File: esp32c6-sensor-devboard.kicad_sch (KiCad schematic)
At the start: 0 parts

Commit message: schem: add esp32-c6 symbol
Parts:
- added C10, C11, C16, C17, C18: 0u1, Capacitor_SMD:C_0402_1005Metric, symbol Device:C
- added C13: 10n, Capacitor_SMD:C_0402_1005Metric, symbol Device:C
- added C14, C15, C9: 1u, Capacitor_SMD:C_0402_1005Metric, symbol Device:C
- added C8: 10u, Capacitor_SMD:C_0402_1005Metric, symbol Device:C
- added L2: 2n7, Inductor_SMD:L_0402_1005Metric, symbol Device:L
- added U1: ESP32-C6, Package_DFN_QFN:QFN-40-1EP_5x5mm_P0.4mm_EP3.6x3.6mm, symbol PCM_Espressif:ESP32-C6
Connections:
- new net: C11.1, L2.2, U1.2 (VDDA3P3), U1.3 (VDDA3P3)
- new net +3V3: C10.1, C13.1, C14.1, C17.1, C18.1, C8.1, C9.1, L2.1, U1.28 (VDDPST2), U1.37 (VDDA1), U1.40 (VDDA2), U1.5 (VDDPST1)
- new net GND: C10.2, C11.2, C13.2, C14.2, C15.2, C16.2, C17.2, C18.2, C8.2, C9.2, U1.41 (GND)
- new net VDD_SPI: C15.1, C16.1, U1.23 (VDD_SPI/GPIO27)

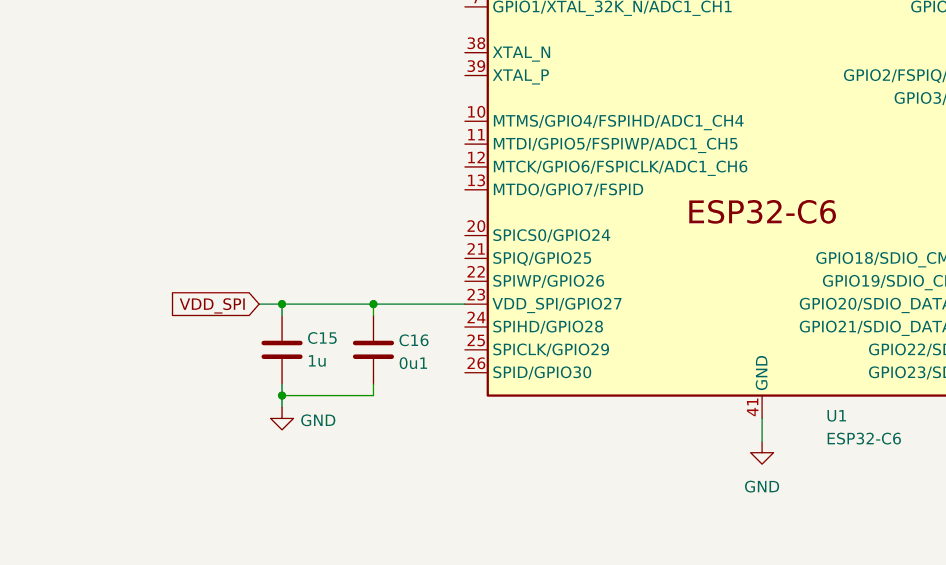
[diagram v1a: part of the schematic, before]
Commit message: schem: add W25Q128JVS 16MB flash
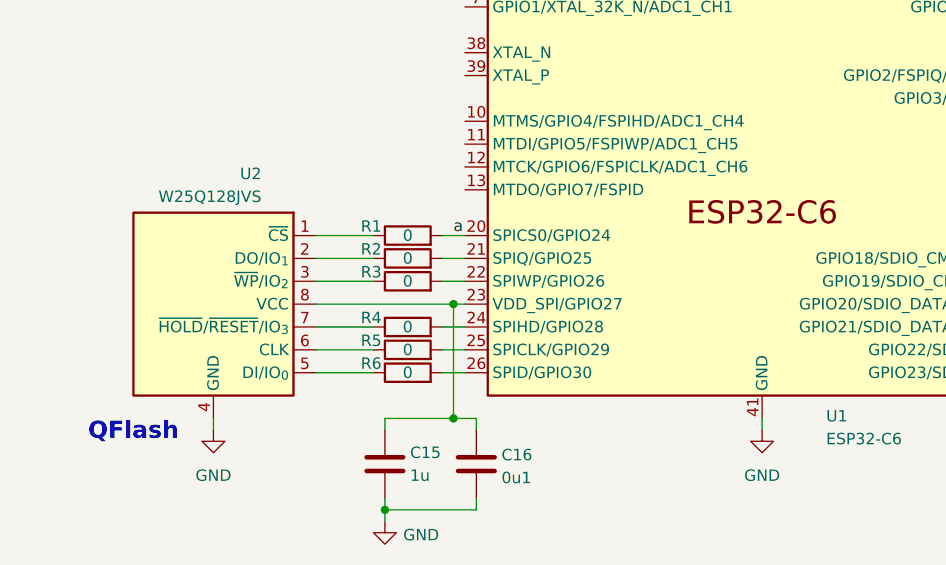
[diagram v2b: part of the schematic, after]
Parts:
- added R1, R2, R3, R4, R5, R6: 0, symbol Device:R
- added U2: W25Q128JVS, Package_SO:SOIC-8_5.3x5.3mm_P1.27mm, symbol Memory_Flash:W25Q128JVS
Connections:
- net GND: now also U2.4 (GND)
- net a: now reaches U1.20 (SPICS0/GPIO24)
- net a: now also R1.2
- net at U1.21 (SPIQ/GPIO25): now also R2.2
- net at U1.22 (SPIWP/GPIO26): now also R3.2
- net at U1.24 (SPIHD/GPIO28): now also R4.2
- net at U1.25 (SPICLK/GPIO29): now also R5.2
- net at U1.26 (SPID/GPIO30): now also R6.2
- net VDD_SPI: no longer names the net of C15.1, C16.1, U1.23 (VDD_SPI/GPIO27)
- net VDD_SPI: now also U2.8 (VCC)
- new net: R2.1, U2.2 (DO/IO_{1})
- new net: R5.1, U2.6 (CLK)
- new net: R1.1, U2.1 (~{CS})
- new net: R3.1, U2.3 (~{WP}/IO_{2})
- new net: R6.1, U2.5 (DI/IO_{0})
- new net: R4.1, U2.7 (~{HOLD}/~{RESET}/IO_{3})
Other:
- note added: "QFlash"
- moved on the sheet: C15, C16

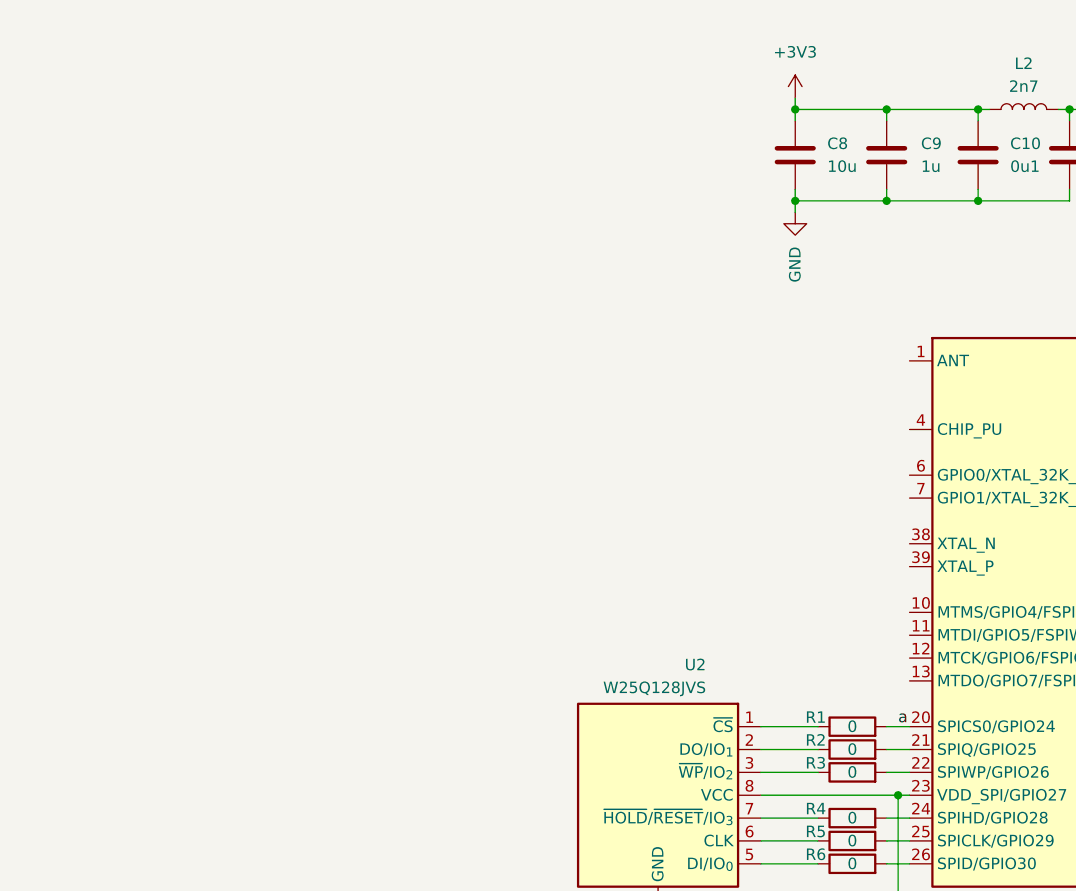
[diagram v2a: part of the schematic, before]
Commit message: schem: add low and high speed crystals
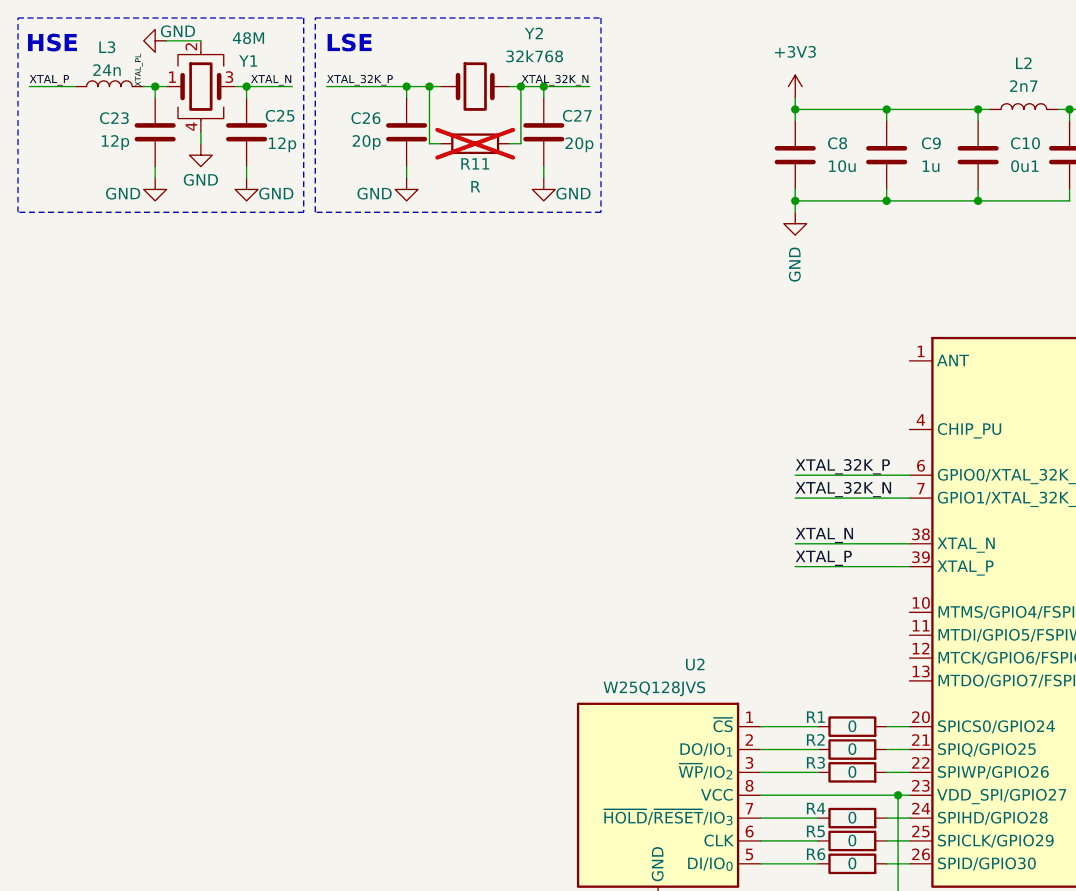
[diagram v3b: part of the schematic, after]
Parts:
- added C23, C25: 12p, Capacitor_SMD:C_0402_1005Metric, symbol Device:C
- added C26, C27: 20p, Capacitor_SMD:C_0402_1005Metric, symbol Device:C
- added L3: 24n, Inductor_SMD:L_0402_1005Metric, symbol Device:L
- added R11: R, Resistor_SMD:R_0603_1608Metric, symbol Device:R
- added Y1: 48M, Crystal:Crystal_SMD_2016-4Pin_2.0x1.6mm, symbol Device:Crystal_GND24
- added Y2: 32k768, Crystal:Crystal_SMD_3215-2Pin_3.2x1.5mm, symbol Device:Crystal
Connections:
- net GND: now also C23.1, C25.2, C26.1, C27.2, Y1.2, Y1.4
- net XTAL_N: now reaches U1.38 (XTAL_N)
- net XTAL_N: now also C25.1, Y1.3
- net XTAL_P: now reaches U1.39 (XTAL_P)
- net XTAL_P: now also L3.1
- net XTAL_32K_P: now reaches U1.6 (GPIO0/XTAL_32K_P/ADC1_CH0)
- net XTAL_32K_P: now also C26.2, R11.1, Y2.1
- net XTAL_32K_N: now reaches U1.7 (GPIO1/XTAL_32K_N/ADC1_CH1)
- net XTAL_32K_N: now also C27.1, R11.2, Y2.2
- net a: no longer names the net of R1.2, U1.20 (SPICS0/GPIO24)
- new net XTAL_PL: C23.2, L3.2, Y1.1
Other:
- note added: "HSE"
- note added: "LSE"

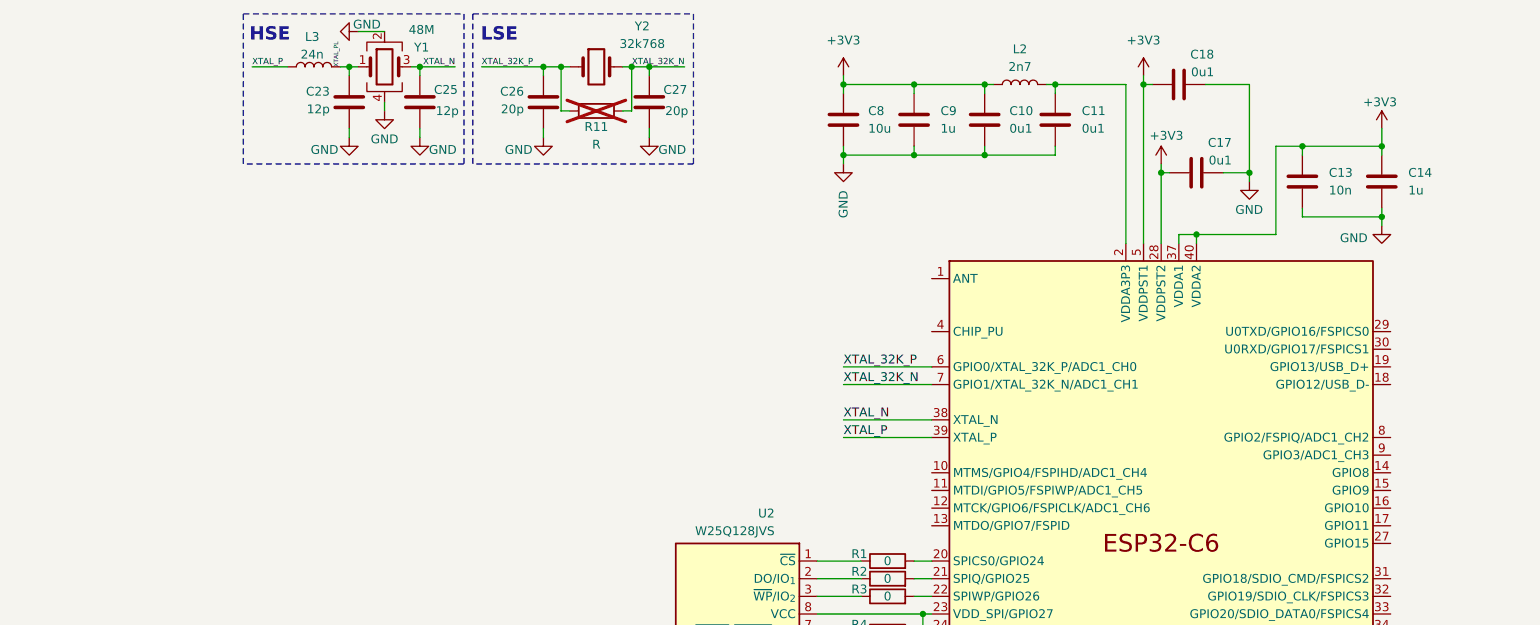
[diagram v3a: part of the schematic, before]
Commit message: schem: add strapping pins and btns
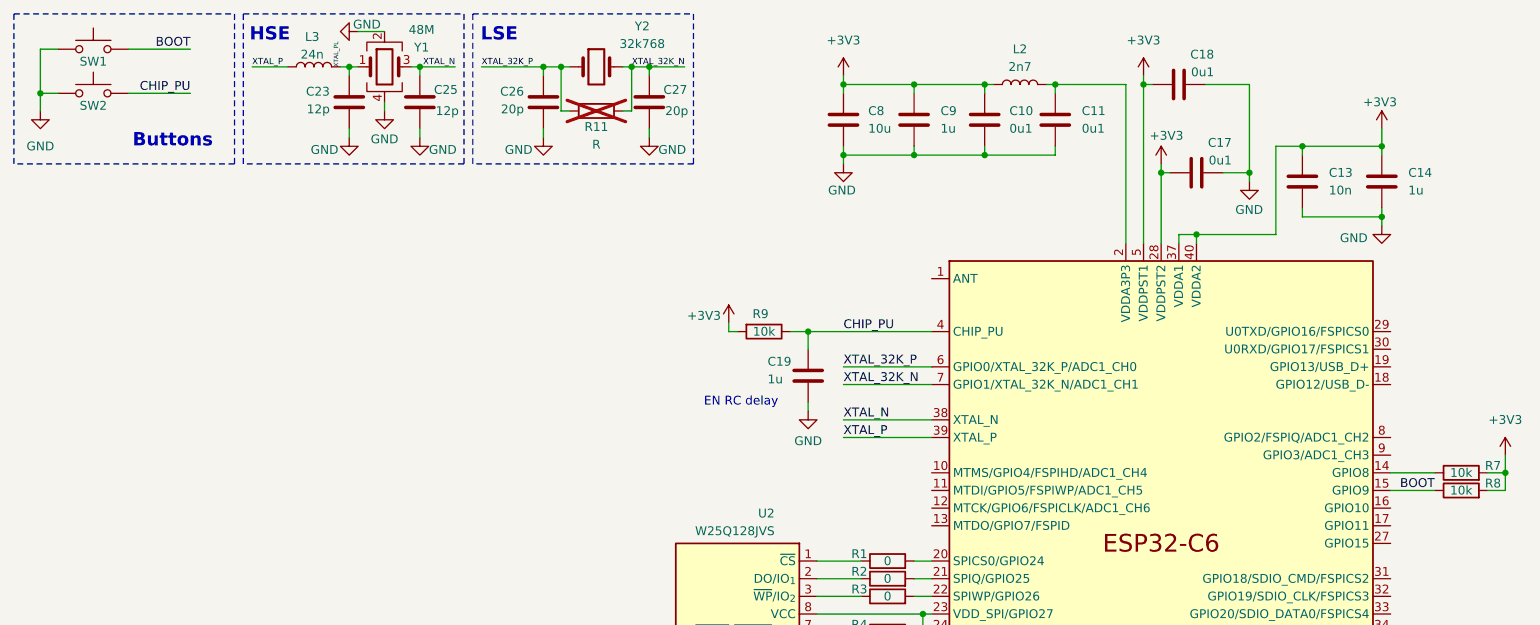
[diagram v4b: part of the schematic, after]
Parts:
- added C19: 1u, Capacitor_SMD:C_0402_1005Metric, symbol Device:C
- added R7, R8, R9: 10k, Resistor_SMD:R_0603_1608Metric, symbol Device:R
- added SW1, SW2: SW_Push, Button_Switch_THT:SW_SPST_Omron_B3F-40xx, symbol Switch:SW_Push
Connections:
- net +3V3: now also R7.2, R8.2, R9.2
- net GND: now also C19.2, SW1.1, SW2.1
- net at U1.14 (GPIO8): now also R7.1
- net BOOT: now reaches U1.15 (GPIO9)
- net BOOT: now also R8.1, SW1.2
- net CHIP_PU: now reaches U1.4 (CHIP_PU)
- net CHIP_PU: now also C19.1, R9.1, SW2.2
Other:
- note added: "Buttons"
- note added: "EN RC delay"

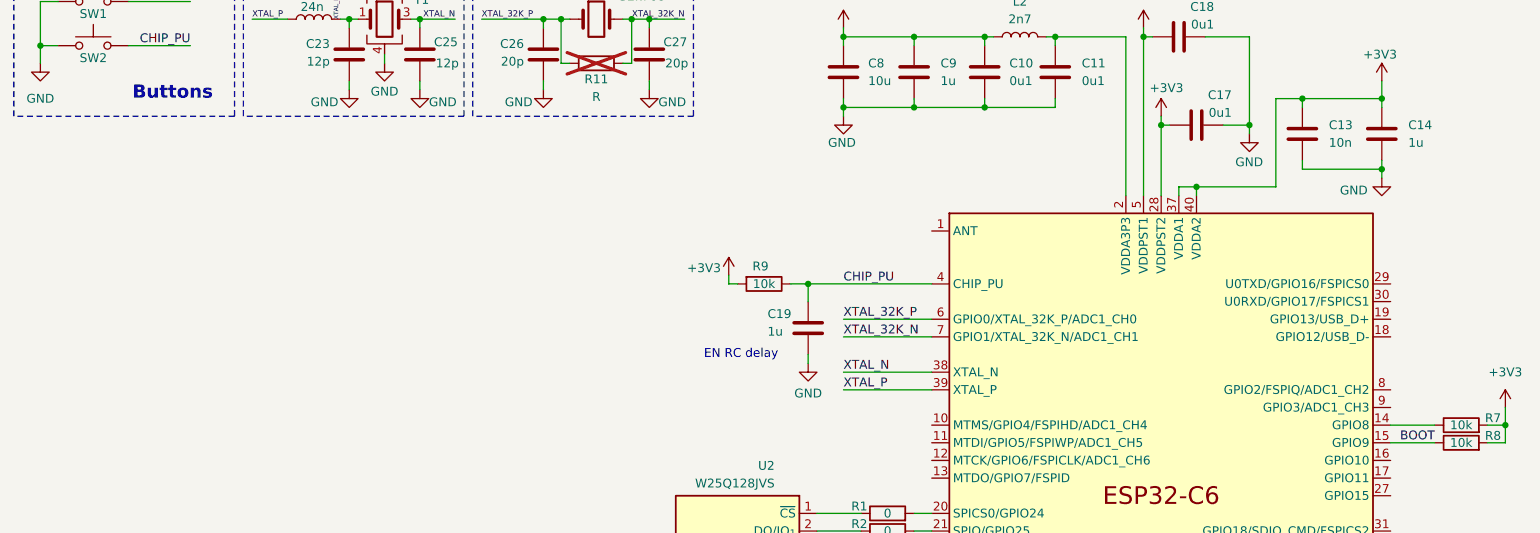
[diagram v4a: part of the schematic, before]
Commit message: schem: add usb c connector
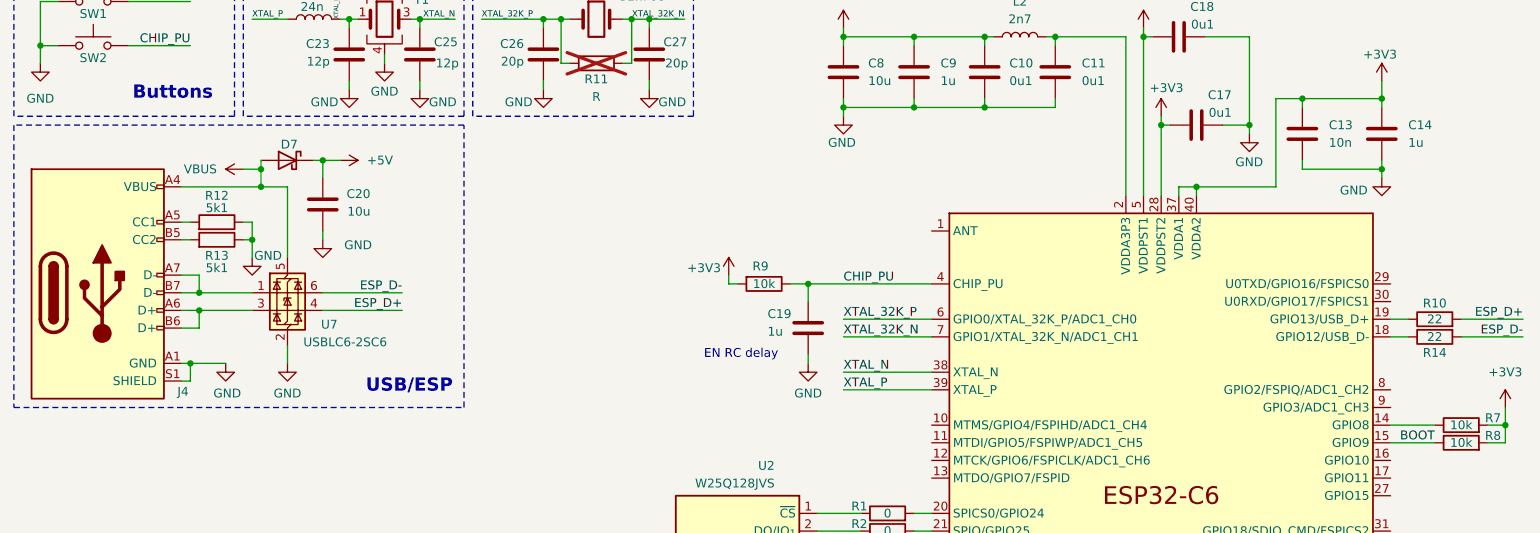
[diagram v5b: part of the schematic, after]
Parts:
- added C20: 10u, Capacitor_SMD:C_0402_1005Metric, symbol Device:C
- added D7: D_Schottky, Diode_SMD:D_SMA, symbol Device:D_Schottky
- added J4: USB_C_Receptacle_USB2.0_14P, Connector_USB:USB_C_Receptacle_HRO_TYPE-C-31-M-12, symbol Connector:USB_C_Receptacle_USB2.0_14P
- added R10, R14: 22, symbol Device:R
- added R12, R13: 5k1, Resistor_SMD:R_0603_1608Metric, symbol Device:R
- added U7: USBLC6-2SC6, Package_TO_SOT_SMD:SOT-23-6, symbol Power_Protection:USBLC6-2SC6
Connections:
- net GND: now also C20.2, J4.A1 (GND), J4.S1 (SHIELD), R12.1, R13.1, U7.2 (GND)
- net at U1.18 (GPIO12/USB_D-): now also R14.1
- net at U1.19 (GPIO13/USB_D+): now also R10.1
- new net: J4.A5 (CC1), R12.2
- new net: J4.A6 (D+), J4.B6 (D+), U7.3 (I/O2)
- new net: J4.A7 (D-), J4.B7 (D-), U7.1 (I/O1)
- new net: J4.A9 (VBUS), J4.B4 (VBUS), J4.B9 (VBUS)
- new net: J4.B1 (GND), J4.B12 (GND)
- new net: J4.B5 (CC2), R13.2
- new net +5V: C20.1, D7.1 (K)
- new net ESP_D+: R10.2, U7.4 (I/O2)
- new net ESP_D-: R14.2, U7.6 (I/O1)
- new net VBUS: D7.2 (A), J4.A4 (VBUS), U7.5 (VBUS)
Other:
- note added: "USB/ESP"

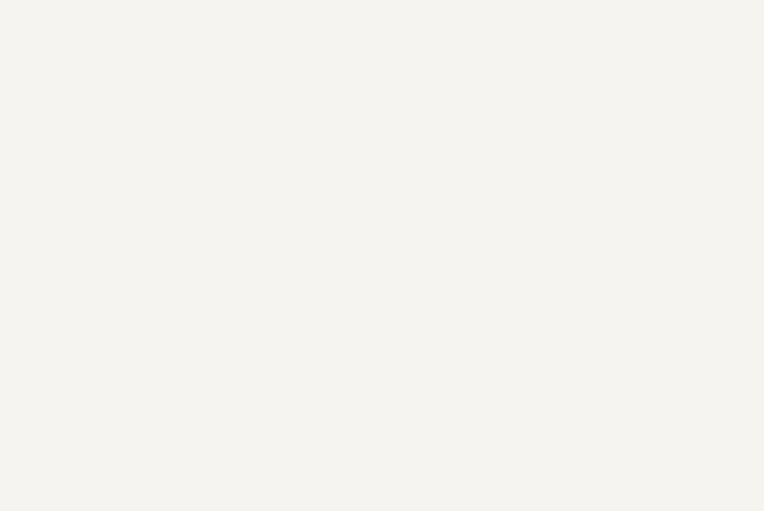
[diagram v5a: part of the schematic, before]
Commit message: schem: add AP2112K 3.3v ldo regulator
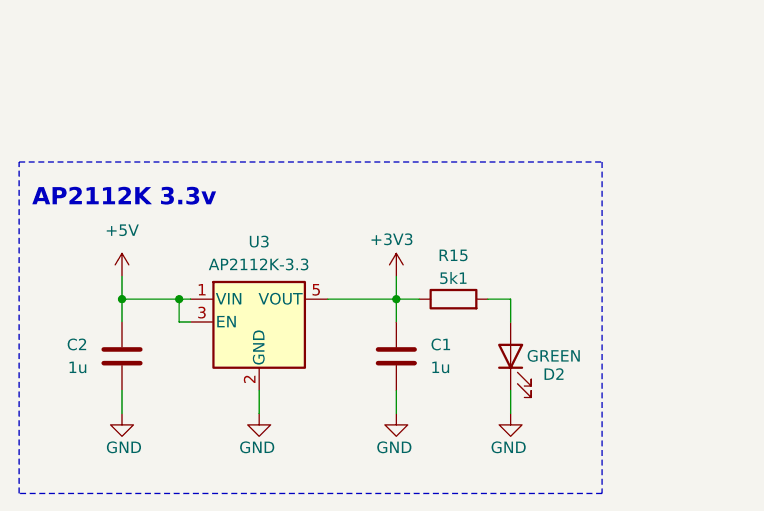
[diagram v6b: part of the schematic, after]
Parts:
- added C1, C2: 1u, symbol Device:C
- added D2: GREEN, LED_SMD:LED_0805_2012Metric, symbol Device:LED
- added R15: 5k1, symbol Device:R
- added U3: AP2112K-3.3, Package_TO_SOT_SMD:SOT-23-5, symbol Regulator_Linear:AP2112K-3.3
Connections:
- net +3V3: now also C1.1, R15.1, U3.5 (VOUT)
- net +5V: now also C2.1, U3.1 (VIN), U3.3 (EN)
- net GND: now also C1.2, C2.2, D2.1 (K), U3.2 (GND)
- new net: D2.2 (A), R15.2
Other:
- note added: "AP2112K 3.3v"

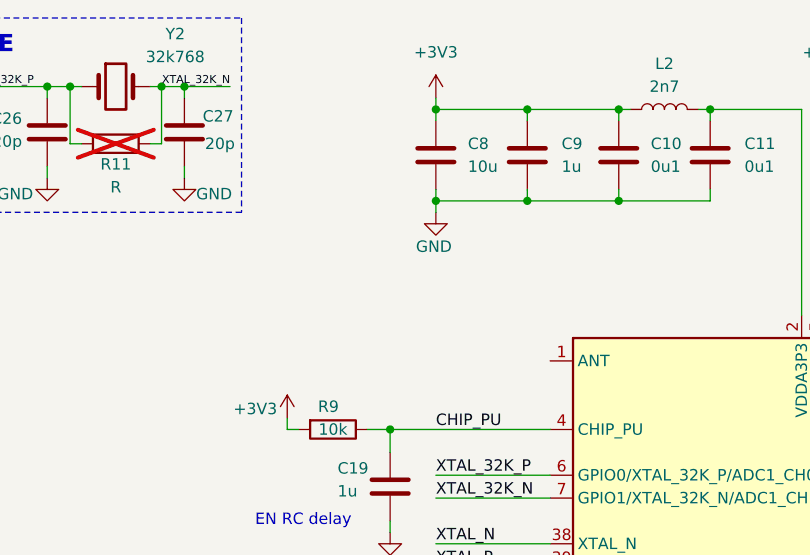
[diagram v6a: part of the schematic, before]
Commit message: schem: add rf antenna
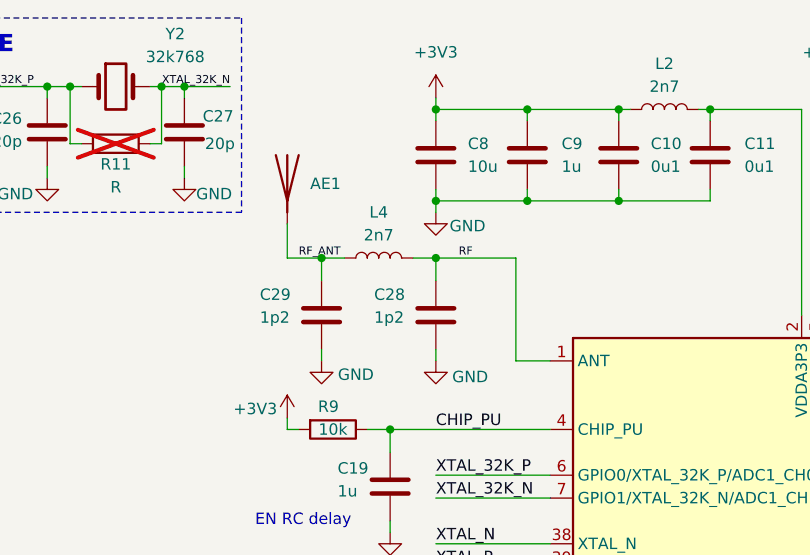
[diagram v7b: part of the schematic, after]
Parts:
- added AE1: Antenna, symbol Device:Antenna
- added C28, C29: 1p2, Capacitor_SMD:C_0402_1005Metric, symbol Device:C
- added L4: 2n7, Inductor_SMD:L_0402_1005Metric, symbol Device:L
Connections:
- net GND: now also C28.2, C29.2
- net RF: now reaches U1.1 (ANT)
- net RF: now also C28.1, L4.2
- new net RF_ANT: AE1.1 (A), C29.1, L4.1

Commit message: schem: clean up
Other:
- note added: "Power"
- moved on the sheet: C15, C16, C20, C23, C25, C26, C27, D7, J4, L3, R11, R12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
